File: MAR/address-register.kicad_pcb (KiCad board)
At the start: 2 copper layers, 72.4 x 50.8 mm, 39 parts, among them J1 Power, J2 Bus, J3 Misc, J4 Address, SW1 SW_DIP_x04, SW2 SW_DPDT_x2, U1 74LS173, U2 74LS157

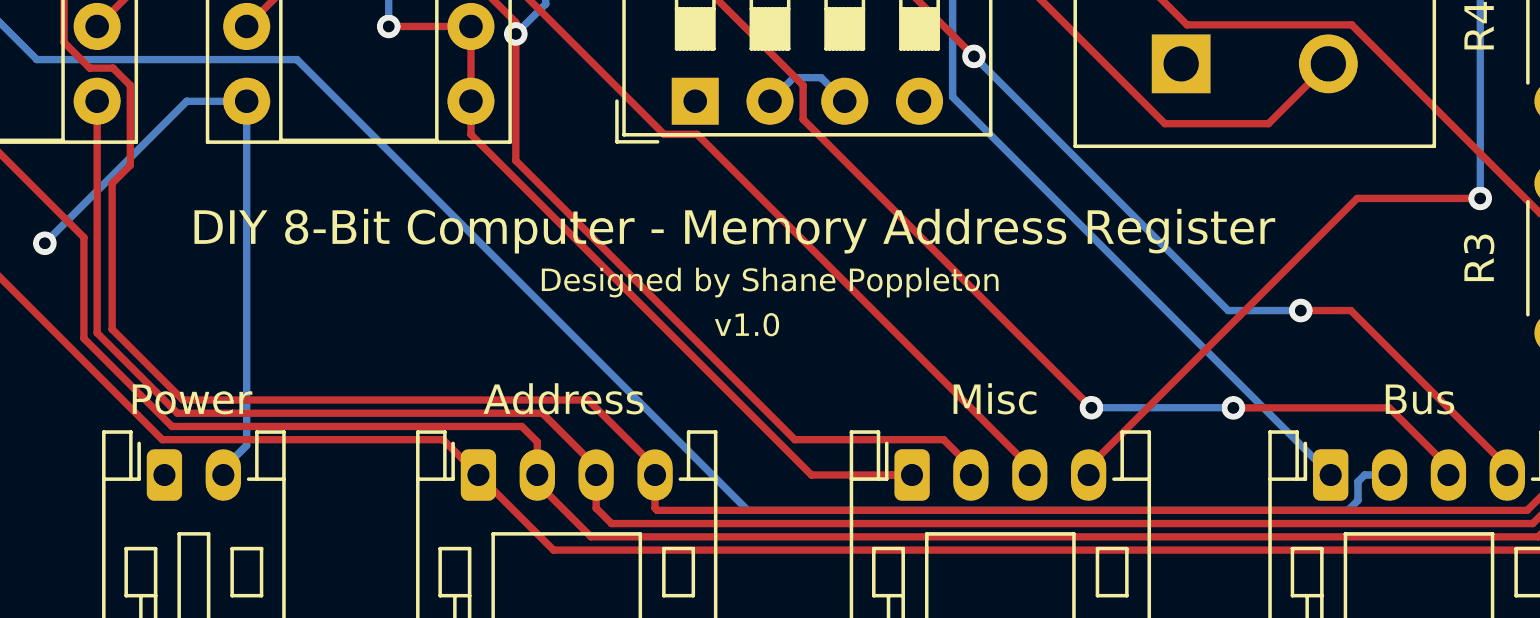
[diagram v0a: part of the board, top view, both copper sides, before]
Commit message: Added Attribution on each PCB, and regenerated gerbers
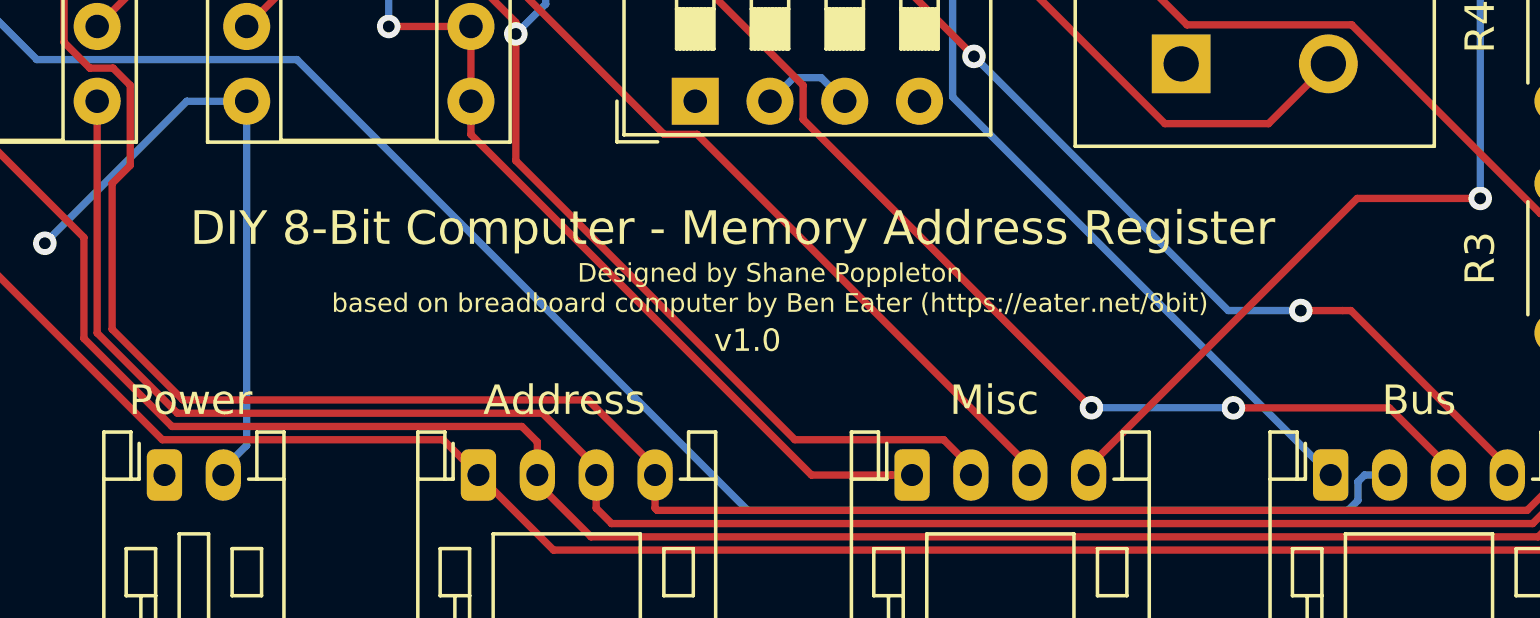
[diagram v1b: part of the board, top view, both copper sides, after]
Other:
- board text added: "Designed by Shane Poppleton based on breadboard computer by Ben Eater (https://eater.net/8bit)"
- board text removed: "Designed by Shane Poppleton"
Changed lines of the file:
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@@
       (net 1 +5V))
   )
-  (gr_text v1.0 (at 48.768 55.88) (layer F.SilkS)
+  (gr_text v1.0 (at 48.768 56.388) (layer F.SilkS)
     (effects (font (size 0.762 0.762) (thickness 0.127)))
   )
-  (gr_text "Designed by Shane Poppleton" (at 49.53 54.356) (layer F.SilkS)
-    (effects (font (size 0.762 0.762) (thickness 0.127)))
+  (gr_text "Designed by Shane Poppleton\nbased on breadboard computer by Ben Eater (https://eater.net/8bit)\n" (at 49.53 54.61) (layer F.SilkS)
+    (effects (font (size 0.635 0.635) (thickness 0.1016)))
   )
   (gr_text "DIY 8-Bit Computer - Memory Address Register" (at 48.26 52.578) (layer F.SilkS)
